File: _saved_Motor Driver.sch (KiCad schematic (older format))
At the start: 44 parts, among them CON1 AVR-ISP-6, J1 Conn_01x02, J10 Conn_01x04, J5 Conn_01x04, J7 Conn_01x02, J8 Conn_01x02, J9 Conn_01x03, Q1 IRF3205, Q2 IRF3205, Q3 IRF3205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

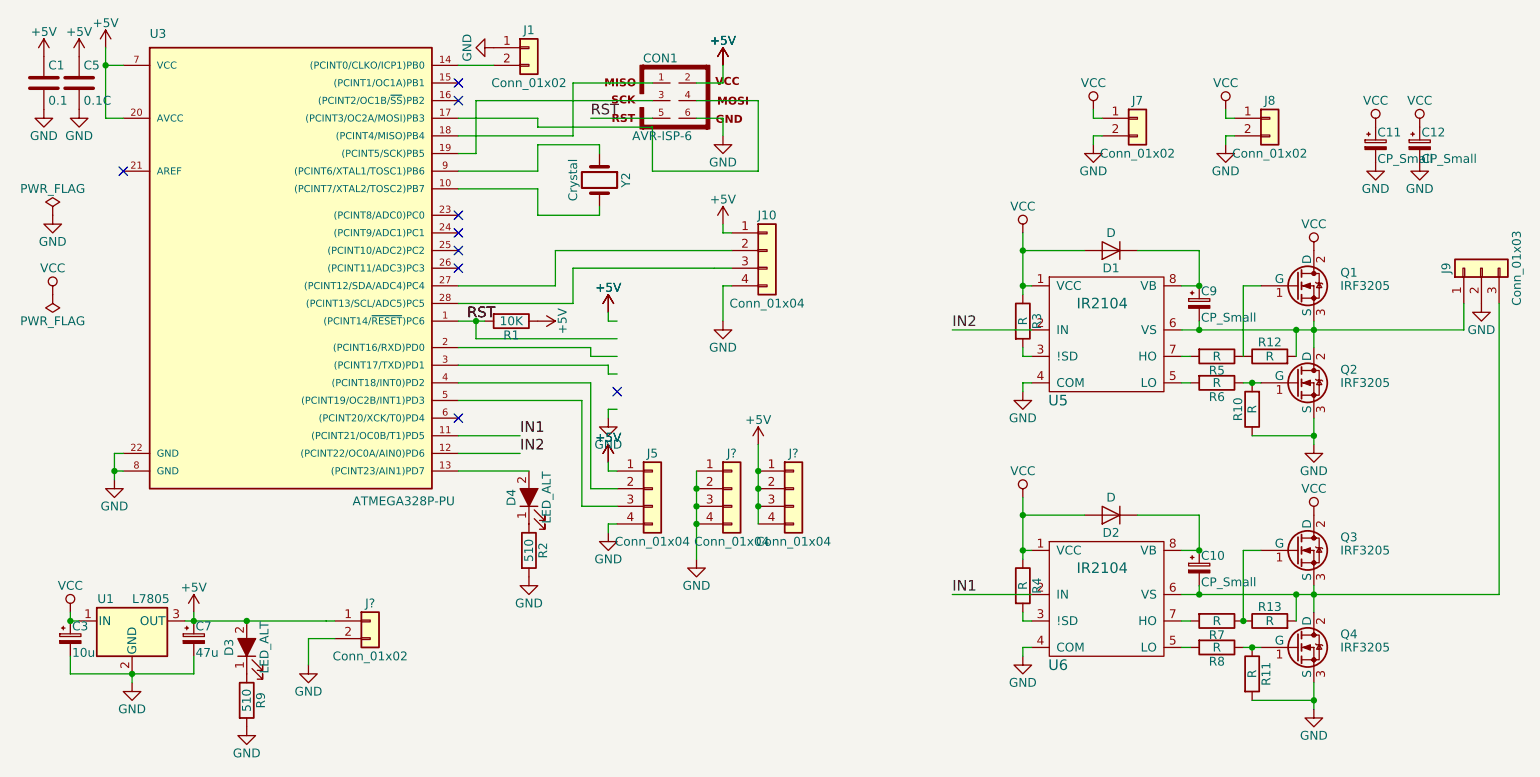
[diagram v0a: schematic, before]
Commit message: Updated SCH|PCB
Updated the SCh for polarity change on the fly using the 2x2 pinheader
PCB was completely newly designed
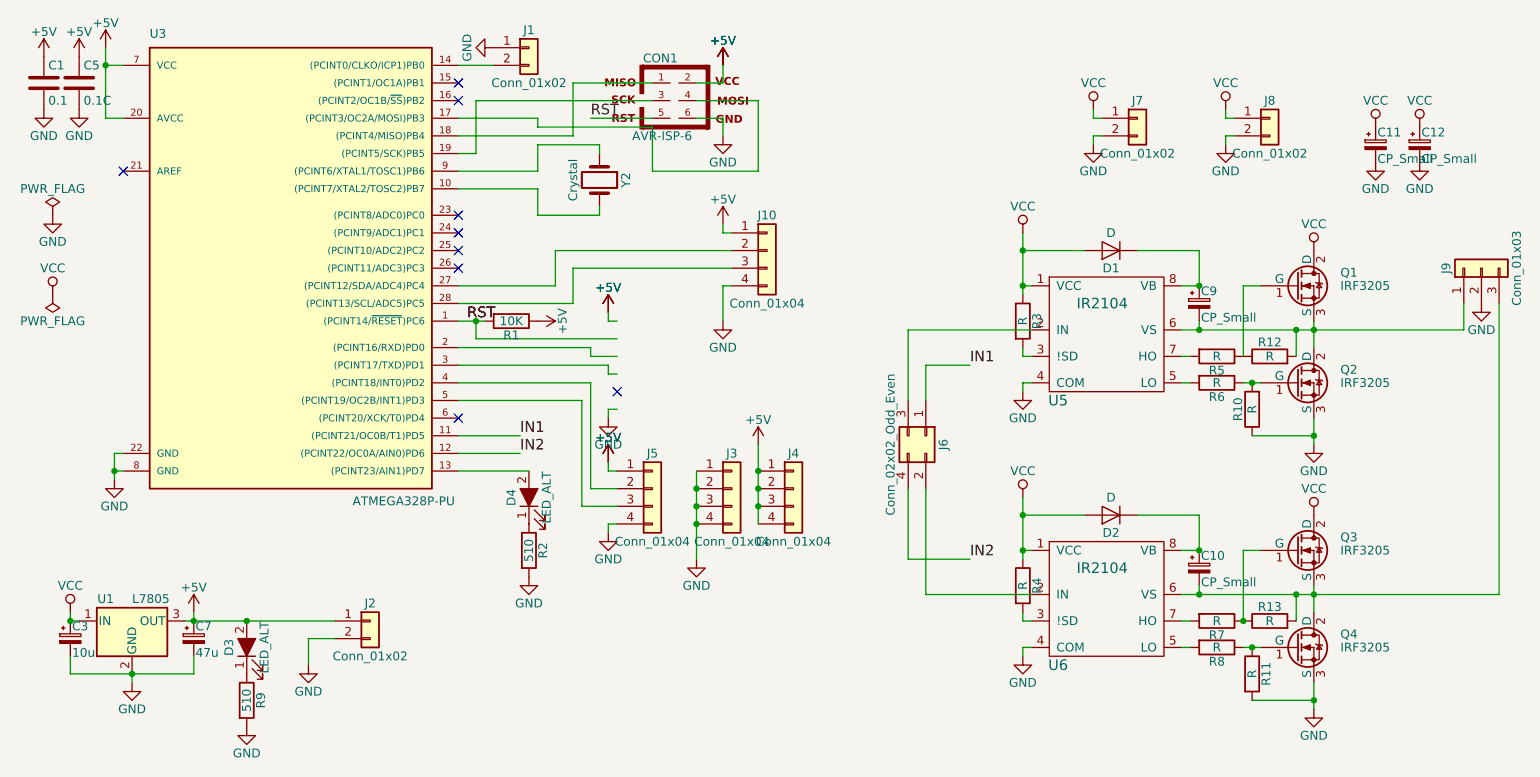
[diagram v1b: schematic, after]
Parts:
- added J6: Conn_02x02_Odd_Even, Pin_Headers:Pin_Header_Straight_2x02_Pitch2.54mm, symbol Conn_02x02_Odd_Even
- gave numbers to parts that had none: 3
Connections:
- wire segments 167 -> 141
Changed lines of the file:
@@
 	1600 3550 1550 3550
 Wire Wire Line
-	1550 3550 1550 3650
-Wire Wire Line
-	1550 3650 1550 3700
+	1550 3550 1550 3700
 Wire Wire Line
 	1600 3650 1550 3650
 Connection ~ 1550 3650
 Wire Wire Line
-	1500 1250 1500 1350
-Wire Wire Line
-	1500 1350 1500 1650
+	1500 1250 1500 1650
 Wire Wire Line
 	1500 1650 1600 1650
@@
 	4300 2200 4300 2150
 Wire Wire Line
-	3500 2800 3600 2800
-Wire Wire Line
-	3600 2800 3650 2800
+	3500 2800 3650 2800
 Wire Wire Line
 	3500 2950 4250 2950
@@
 	1300 4500 1300 4450
 Wire Wire Line
-	1950 4500 2000 4500
-Wire Wire Line
-	2000 4500 2300 4500
-Wire Wire Line
-	2300 4500 2750 4500
+	1950 4500 2800 4500
 Wire Wire Line
 	2000 4500 2000 4450
@@
 	1300 4700 1300 4800
 Wire Wire Line
-	1300 4800 1650 4800
-Wire Wire Line
-	1650 4800 2000 4800
+	1300 4800 2000 4800
 Wire Wire Line
 	2000 4800 2000 4700
@@
 $EndComp
 Wire Wire Line
-	7600 2850 7700 2850
-Wire Wire Line
-	7700 2850 8250 2850
-Wire Wire Line
-	8250 2850 8350 2850
-Wire Wire Line
-	8350 2850 9200 2850
+	7600 2850 9200 2850
 Wire Wire Line
 	7700 2850 7700 2800
 Wire Wire Line
-	8350 2800 8350 2850
-Wire Wire Line
-	8350 2850 8350 2950
+	8350 2800 8350 2950
 Connection ~ 7700 2850
 Connection ~ 8350 2850
@@
 	7600 3150 7650 3150
 Wire Wire Line
-	7950 3150 8000 3150
-Wire Wire Line
-	8000 3150 8050 3150
+	7950 3150 8050 3150
 $Comp
 L VCC #PWR022
@@
 	6700 2600 6750 2600
 Wire Wire Line
-	6700 2300 6700 2400
-Wire Wire Line
-	6700 2400 6700 2600
-Wire Wire Line
-	6700 2600 6700 2650
+	6700 2300 6700 2650
 Wire Wire Line
 	7050 2400 6700 2400
@@
 	7700 2400 7700 2600
 Wire Wire Line
-	6300 2850 6750 2850
+	6050 2850 6750 2850
 $Comp
 L R R3
@@
 Wire Wire Line
 	9200 2850 9200 2700
-Text Label 6300 2850 0    60   ~ 0
-IN2
 Connection ~ 7700 2600
 $Comp
@@
 $EndComp
 Wire Wire Line
-	7600 4350 7700 4350
-Wire Wire Line
-	7700 4350 8250 4350
-Wire Wire Line
-	8250 4350 8350 4350
-Wire Wire Line
-	8350 4350 9400 4350
+	7600 4350 9400 4350
 Wire Wire Line
 	7700 4350 7700 4300
 Wire Wire Line
-	8350 4300 8350 4350
-Wire Wire Line
-	8350 4350 8350 4450
+	8350 4300 8350 4450
 Connection ~ 7700 4350
 Connection ~ 8350 4350
@@
 	7600 4650 7650 4650
 Wire Wire Line
-	7950 4650 8000 4650
-Wire Wire Line
-	8000 4650 8050 4650
+	7950 4650 8050 4650
 $Comp
 L VCC #PWR034
@@
 	6700 4100 6750 4100
 Wire Wire Line
-	6700 3800 6700 3900
-Wire Wire Line
-	6700 3900 6700 4100
-Wire Wire Line
-	6700 4100 6700 4150
+	6700 3800 6700 4150
 Wire Wire Line
 	7050 3900 6700 3900
@@
 	7700 3900 7700 4100
 Wire Wire Line
-	6300 4350 6750 4350
+	6150 4350 6750 4350
 $Comp
 L R R4
@@
 	6700 4500 6700 4450
 Connection ~ 6700 4100
-Text Label 6300 4350 0    60   ~ 0
-IN1
 Connection ~ 7700 4100
 Wire Wire Line
@@
 	4050 2400 5050 2400
 Wire Wire Line
-	5050 2500 4950 2500
-Wire Wire Line
-	4950 2500 4950 2500
-Wire Wire Line
-	4950 2500 4150 2500
+	4150 2500 5050 2500
 Wire Wire Line
 	4150 2500 4150 2700
@@
 	8000 3450 8350 3450
 Wire Wire Line
-	8350 3350 8350 3450
-Wire Wire Line
-	8350 3450 8350 3500
+	8350 3350 8350 3500
 Connection ~ 8350 3450
 Connection ~ 8000 3150
@@
 Connection ~ 8000 4650
 Wire Wire Line
-	8350 5000 8350 4950
-Wire Wire Line
-	8350 4950 8350 4850
+	8350 4850 8350 5000
 Wire Wire Line
 	8350 4950 8000 4950
 Connection ~ 8350 4950
 $Comp
-L Conn_01x04 J?
+L Conn_01x04 J3
 U 1 1 5A2BDE9D
 P 5050 3750
-F 0 "J?" H 5050 3950 50  0000 C CNN
+F 0 "J3" H 5050 3950 50  0000 C CNN
 F 1 "Conn_01x04" H 5050 3450 50  0000 C CNN
 F 2 "Pin_Headers:Pin_Header_Straight_1x04_Pitch2.54mm" H 5050 3750 50  0001 C CNN
@@
 $EndComp
 $Comp
-L Conn_01x04 J?
+L Conn_01x04 J4
 U 1 1 5A2BDF32
 P 5400 3750
-F 0 "J?" H 5400 3950 50  0000 C CNN
+F 0 "J4" H 5400 3950 50  0000 C CNN
 F 1 "Conn_01x04" H 5400 3450 50  0000 C CNN
 F 2 "Pin_Headers:Pin_Header_Straight_1x04_Pitch2.54mm" H 5400 3750 50  0001 C CNN
@@
 $EndComp
 Wire Wire Line
-	4850 3650 4850 3750
-Wire Wire Line
-	4850 3750 4850 3850
-Wire Wire Line
-	4850 3850 4850 3950
-Wire Wire Line
-	4850 3950 4850 4150
+	4850 3650 4850 4150
 Connection ~ 4850 3750
 Connection ~ 4850 3850
 Connection ~ 4850 3950
 Wire Wire Line
-	5200 3950 5200 3850
-Wire Wire Line
-	5200 3850 5200 3750
-Wire Wire Line
-	5200 3750 5200 3650
-Wire Wire Line
-	5200 3650 5200 3500
+	5200 3500 5200 3950
 Connection ~ 5200 3650
 Connection ~ 5200 3750
 Connection ~ 5200 3850
 $Comp
-L GND #PWR?
+L GND #PWR046
 U 1 1 5A2BE1A4
 P 4850 4150
-F 0 "#PWR?" H 4850 3900 50  0001 C CNN
+F 0 "#PWR046" H 4850 3900 50  0001 C CNN
 F 1 "GND" H 4850 4000 50  0000 C CNN
 F 2 "" H 4850 4150 50  0001 C CNN
@@
 $EndComp
 $Comp
-L +5V #PWR?
+L +5V #PWR047
 U 1 1 5A2BE210
 P 5200 3500
-F 0 "#PWR?" H 5200 3350 50  0001 C CNN
+F 0 "#PWR047" H 5200 3350 50  0001 C CNN
 F 1 "+5V" H 5200 3640 50  0000 C CNN
 F 2 "" H 5200 3500 50  0001 C CNN
@@
 $EndComp
 $Comp
-L Conn_01x02 J?
+L Conn_01x02 J2
 U 1 1 5A2BF6B8
 P 3000 4500
-F 0 "J?" H 3000 4600 50  0000 C CNN
+F 0 "J2" H 3000 4600 50  0000 C CNN
 F 1 "Conn_01x02" H 3000 4300 50  0000 C CNN
 F 2 "Pin_Headers:Pin_Header_Straight_1x02_Pitch2.54mm" H 3000 4500 50  0001 C CNN
@@
 	1    0    0    -1
 $EndComp
-Wire Wire Line
-	2750 4500 2750 4500
-Wire Wire Line
-	2750 4500 2800 4500
 Connection ~ 2300 4500
 $Comp
-L GND #PWR?
+L GND #PWR048
 U 1 1 5A2BFA0E
 P 2650 4750
-F 0 "#PWR?" H 2650 4500 50  0001 C CNN
+F 0 "#PWR048" H 2650 4500 50  0001 C CNN
 F 1 "GND" H 2650 4600 50  0000 C CNN
 F 2 "" H 2650 4750 50  0001 C CNN
@@
 Wire Wire Line
 	2650 4600 2650 4750
+$Comp
+L Conn_02x02_Odd_Even J6
+U 1 1 5A2BF2DE
+P 6150 3450
+F 0 "J6" H 6200 3550 50  0000 C CNN
+F 1 "Conn_02x02_Odd_Even" H 6200 3250 50  0000 C CNN
+F 2 "Pin_Headers:Pin_Header_Straight_2x02_Pitch2.54mm" H 6150 3450 50  0001 C CNN
+F 3 "" H 6150 3450 50  0001 C CNN
+	1    6150 3450
+	0    1    1    0
+$EndComp
+Wire Wire Line
+	6150 4350 6150 3750
+Wire Wire Line
+	6050 3250 6050 2850
+Wire Wire Line
+	6150 3250 6150 3050
+Wire Wire Line
+	6150 3050 6400 3050
+Wire Wire Line
+	6050 3750 6050 4150
+Wire Wire Line
+	6050 4150 6400 4150
+Text Label 6400 3050 0    60   ~ 0
+IN1
+Text Label 6400 4150 0    60   ~ 0
+IN2
 $EndSCHEMATC
